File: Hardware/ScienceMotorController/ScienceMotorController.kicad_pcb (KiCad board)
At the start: 2 copper layers, 125.7 x 166.4 mm, 148 parts, among them U1 VNH5019A_E, U10 PMN280ENEAX, U11 PMN280ENEAX, U12 LT1910, U13 LT1910, U14 LT1910, U15 5VA OKI, U2 VNH5019A_E, U3 VNH5019A_E, U4 VNH5019A_E, U5 5V OKI, U6 TM4C129E_Launchpad, U7 3V3 OKI, U8 5VA OKI, U9 PMN280ENEAX

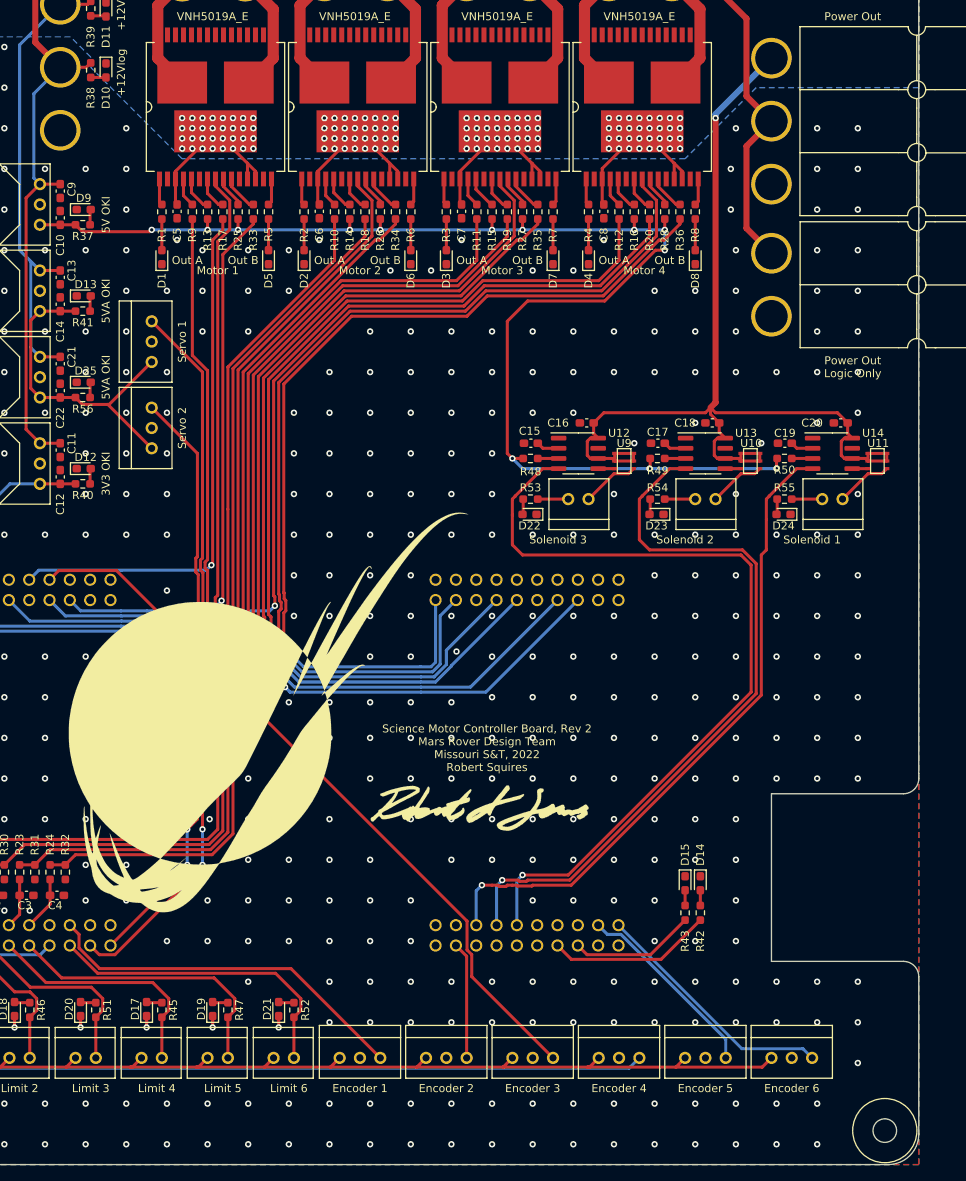
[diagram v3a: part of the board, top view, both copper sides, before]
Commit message: 9 Solenoids, Fixed PWM Overlap
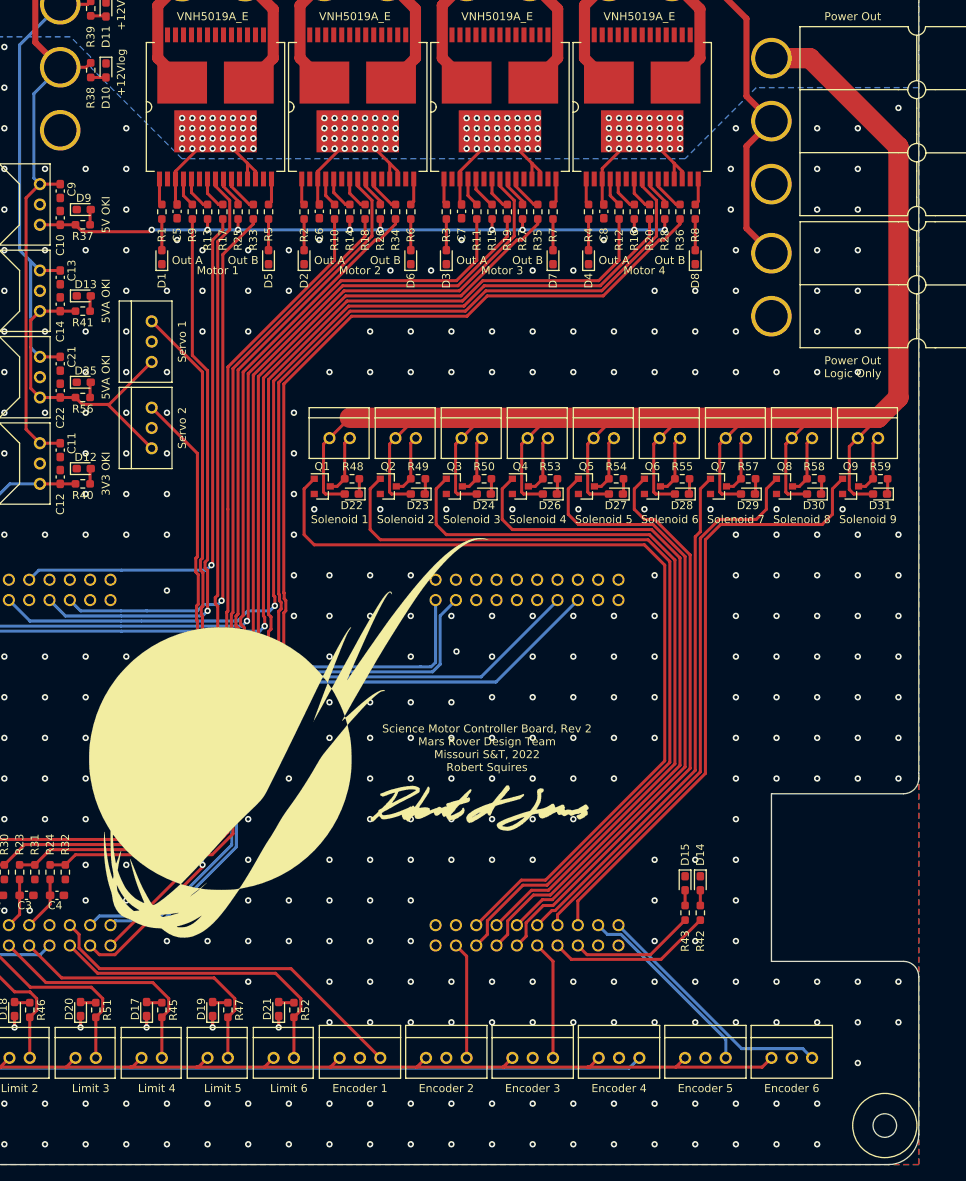
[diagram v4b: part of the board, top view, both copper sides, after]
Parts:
- removed C15, C17, C19: 0.1 uF, Capacitor_SMD:C_0603_1608Metric_Pad1.08x0.95mm_HandSolder
- removed C16, C18, C20: 10uF 50V, Capacitor_SMD:C_0603_1608Metric_Pad1.08x0.95mm_HandSolder
- removed SolValve1, SolValve2, SolValve3: Molex_SL_02, MRDT_Connectors:MOLEX_SL_02_Vertical
- removed U10, U11, U9: PMN280ENEAX, Mosfet:PMN280ENEAX
- removed U12, U13, U14: LT1910, Package_SO:SOIC-8_3.9x4.9mm_P1.27mm
- added D26: LED, LED_SMD:LED_0603_1608Metric_Pad1.05x0.95mm_HandSolder, F.Cu at (113.9, 43.2)
- added D27: LED, LED_SMD:LED_0603_1608Metric_Pad1.05x0.95mm_HandSolder, F.Cu at (122.2, 43.2)
- added D28: LED, LED_SMD:LED_0603_1608Metric_Pad1.05x0.95mm_HandSolder, F.Cu at (130.4, 43.2)
- added D29: LED, LED_SMD:LED_0603_1608Metric_Pad1.05x0.95mm_HandSolder, F.Cu at (138.7, 43.2)
- added D30: LED, LED_SMD:LED_0603_1608Metric_Pad1.05x0.95mm_HandSolder, F.Cu at (146.9, 43.2)
- added D31: LED, LED_SMD:LED_0603_1608Metric_Pad1.05x0.95mm_HandSolder, F.Cu at (155.2, 43.2)
- added Q1: BSS138, Package_TO_SOT_SMD:SOT-23, F.Cu at (85.5, 42.2)
- added Q2: BSS138, Package_TO_SOT_SMD:SOT-23, F.Cu at (93.7, 42.2)
- added Q3: BSS138, Package_TO_SOT_SMD:SOT-23, F.Cu at (102.0, 42.2)
- added Q4: BSS138, Package_TO_SOT_SMD:SOT-23, F.Cu at (110.2, 42.2)
- added Q5: BSS138, Package_TO_SOT_SMD:SOT-23, F.Cu at (118.5, 42.2)
- added Q6: BSS138, Package_TO_SOT_SMD:SOT-23, F.Cu at (126.7, 42.2)
- added Q7: BSS138, Package_TO_SOT_SMD:SOT-23, F.Cu at (135.0, 42.2)
- added Q8: BSS138, Package_TO_SOT_SMD:SOT-23, F.Cu at (143.2, 42.2)
- added Q9: BSS138, Package_TO_SOT_SMD:SOT-23, F.Cu at (151.5, 42.2)
- added R57: 1k, Resistor_SMD:R_0603_1608Metric_Pad0.98x0.95mm_HandSolder, F.Cu at (138.7, 41.3)
- added R58: 1k, Resistor_SMD:R_0603_1608Metric_Pad0.98x0.95mm_HandSolder, F.Cu at (147.0, 41.3)
- added R59: 1k, Resistor_SMD:R_0603_1608Metric_Pad0.98x0.95mm_HandSolder, F.Cu at (155.2, 41.3)
- added SolVal1: Molex_SL_02, MRDT_Connectors:MOLEX_SL_02_Vertical, F.Cu at (86.4, 36.2)
- added SolVal2: Molex_SL_02, MRDT_Connectors:MOLEX_SL_02_Vertical, F.Cu at (94.6, 36.2)
- added SolVal3: Molex_SL_02, MRDT_Connectors:MOLEX_SL_02_Vertical, F.Cu at (102.9, 36.2)
- added SolVal4: Molex_SL_02, MRDT_Connectors:MOLEX_SL_02_Vertical, F.Cu at (111.1, 36.2)
- added SolVal5: Molex_SL_02, MRDT_Connectors:MOLEX_SL_02_Vertical, F.Cu at (119.4, 36.2)
- added SolVal6: Molex_SL_02, MRDT_Connectors:MOLEX_SL_02_Vertical, F.Cu at (127.6, 36.2)
- added SolVal7: Molex_SL_02, MRDT_Connectors:MOLEX_SL_02_Vertical, F.Cu at (135.9, 36.2)
- added SolVal8: Molex_SL_02, MRDT_Connectors:MOLEX_SL_02_Vertical, F.Cu at (144.1, 36.2)
- added SolVal9: Molex_SL_02, MRDT_Connectors:MOLEX_SL_02_Vertical, F.Cu at (152.4, 36.2)
- R1, R2, R3, R4, R5, R6, R7, R8: value 1.5k -> 1k
- R48, R49, R50: value 5.1k -> 1k
- R53, R54, R55: value 130 -> 1k
- moved R50 37.6 mm to (105.7, 41.3)
- moved D24 37.6 mm to (105.7, 43.2)
- moved R49 30.0 mm to (97.4, 41.3)
- moved D23 30.0 mm to (97.4, 43.2)
- moved R48 22.4 mm to (89.2, 41.3)
- moved D22 22.4 mm to (89.1, 43.2)
- moved R55 13.0 mm to (130.5, 41.3), turned to 180 degrees
- moved R54 5.75 mm to (122.2, 41.3), turned to 180 degrees
- moved G*** 4.07 mm to (81.3, 73.7)
- moved R53 3.54 mm to (113.9, 41.3), turned to 180 degrees
- moved REF** 0.64 mm to (151.8, 118.1)
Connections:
- D22 pad 1: GND -> Net-(D22-Pad1)
- D22 pad 2: Net-(D22-Pad2) -> +12VA
- D23 pad 1: GND -> Net-(D23-Pad1)
- D23 pad 2: Net-(D23-Pad2) -> +12VA
- D24 pad 1: GND -> Net-(D24-Pad1)
- D24 pad 2: Net-(D24-Pad2) -> +12VA
- R48 pad 1: Net-(R48-Pad1) -> Net-(D22-Pad1)
- R48 pad 2: +5V -> Net-(Q1-Pad3)
- R49 pad 1: Net-(R49-Pad1) -> Net-(D23-Pad1)
- R49 pad 2: +5V -> Net-(Q2-Pad3)
- R50 pad 1: Net-(R50-Pad1) -> Net-(D24-Pad1)
- R50 pad 2: +5V -> Net-(Q3-Pad3)
- R53 pad 1: Net-(D22-Pad2) -> Net-(D26-Pad1)
- R54 pad 1: Net-(D23-Pad2) -> Net-(D27-Pad1)
- R55 pad 1: Net-(D24-Pad2) -> Net-(D28-Pad1)
- U6 pad PB5: Solenoid_Valve_2 -> Solenoid_Valve_3
- U6 pad PD0: Encoder_PWM_3 -> Net-(U6-PadPD0)
- U6 pad PD4: Net-(U6-PadPD4) -> Solenoid_Valve_6
- U6 pad PD5: Net-(U6-PadPD5) -> Encoder_PWM_3
- U6 pad PK0: Solenoid_Valve_3 -> Solenoid_Valve_5
- U6 pad PK1: Net-(U6-PadPK1) -> Solenoid_Valve_7
- U6 pad PK2: Net-(U6-PadPK2) -> Solenoid_Valve_8
- U6 pad PK3: Net-(U6-PadPK3) -> Solenoid_Valve_9
- U6 pad PM0: PWM_3 -> Net-(U6-PadPM0)
- U6 pad PM1: PWM_2 -> Net-(U6-PadPM1)
- U6 pad PM4: Net-(U6-PadPM4) -> PWM_2
- U6 pad PM5: Net-(U6-PadPM5) -> PWM_3
- U6 pad PP0: Net-(U6-PadPP0) -> Solenoid_Valve_2
- U6 pad PP1: Net-(U6-PadPP1) -> Solenoid_Valve_4
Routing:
- net +12VA: track 272.9 -> 384.2 mm, vias 129 -> 128
- net Solenoid_Valve_4: track 0.00 -> 89.0 mm
- net +5V: track 170.2 -> 89.4 mm, vias 13 -> 9
- net Encoder_PWM_3: track 92.4 -> 14.9 mm, vias 2 -> 0
- net Solenoid_Valve_5: track 0.00 -> 77.3 mm
- net Solenoid_Valve_9: track 0.00 -> 76.9 mm
- net Solenoid_Valve_6: track 0.00 -> 72.2 mm
- net Solenoid_Valve_8: track 0.00 -> 69.9 mm
- net Solenoid_Valve_7: track 0.00 -> 65.0 mm
- net Solenoid_Valve_1: track 82.4 -> 110.7 mm, vias 1 -> 0
- net Solenoid_Valve_2: track 92.0 -> 105.8 mm, vias 1 -> 0
- net Solenoid_Valve_3: track 104.6 -> 94.1 mm, vias 1 -> 0
- net PWM_3: track 112.4 -> 120.7 mm
- net Net-(Q2-Pad3): track 0.00 -> 7.55 mm
- net Net-(Q1-Pad3): track 0.00 -> 7.55 mm
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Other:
- board text added: "Solenoid 4"
- board text added: "Solenoid 5"
- board text added: "Solenoid 6"
- board text added: "Solenoid 7"
- board text added: "Solenoid 8"
- board text added: "Solenoid 9"

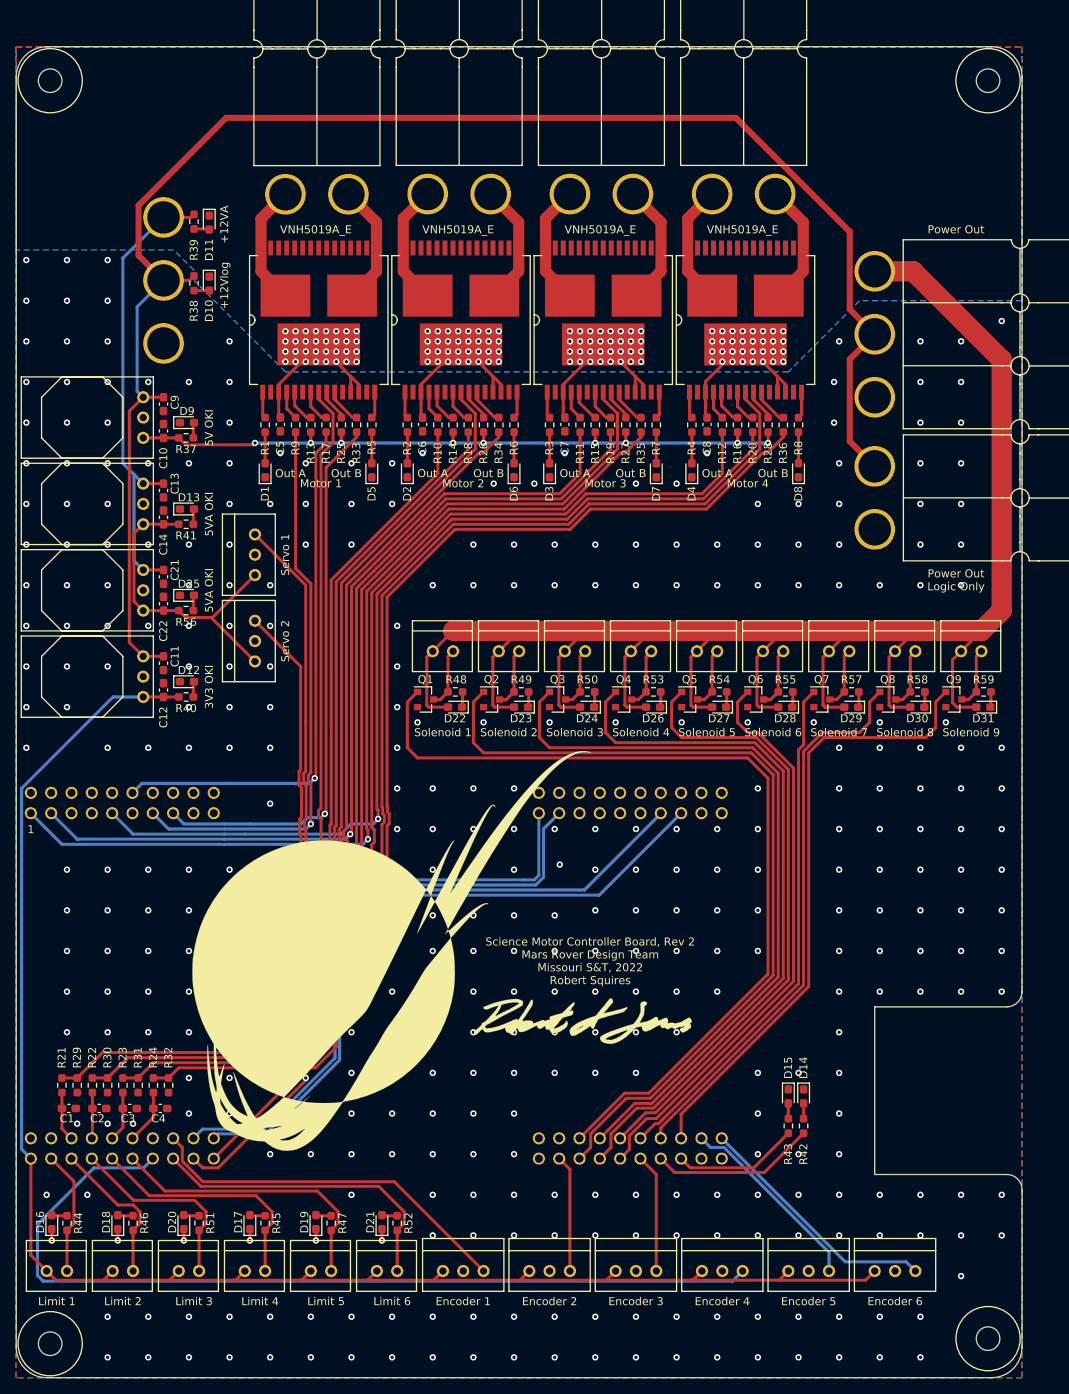
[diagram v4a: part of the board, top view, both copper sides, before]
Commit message: Removed 5V Oki, Moved +12V Passthrough Trace, Added Zener Diodes for Current Sense
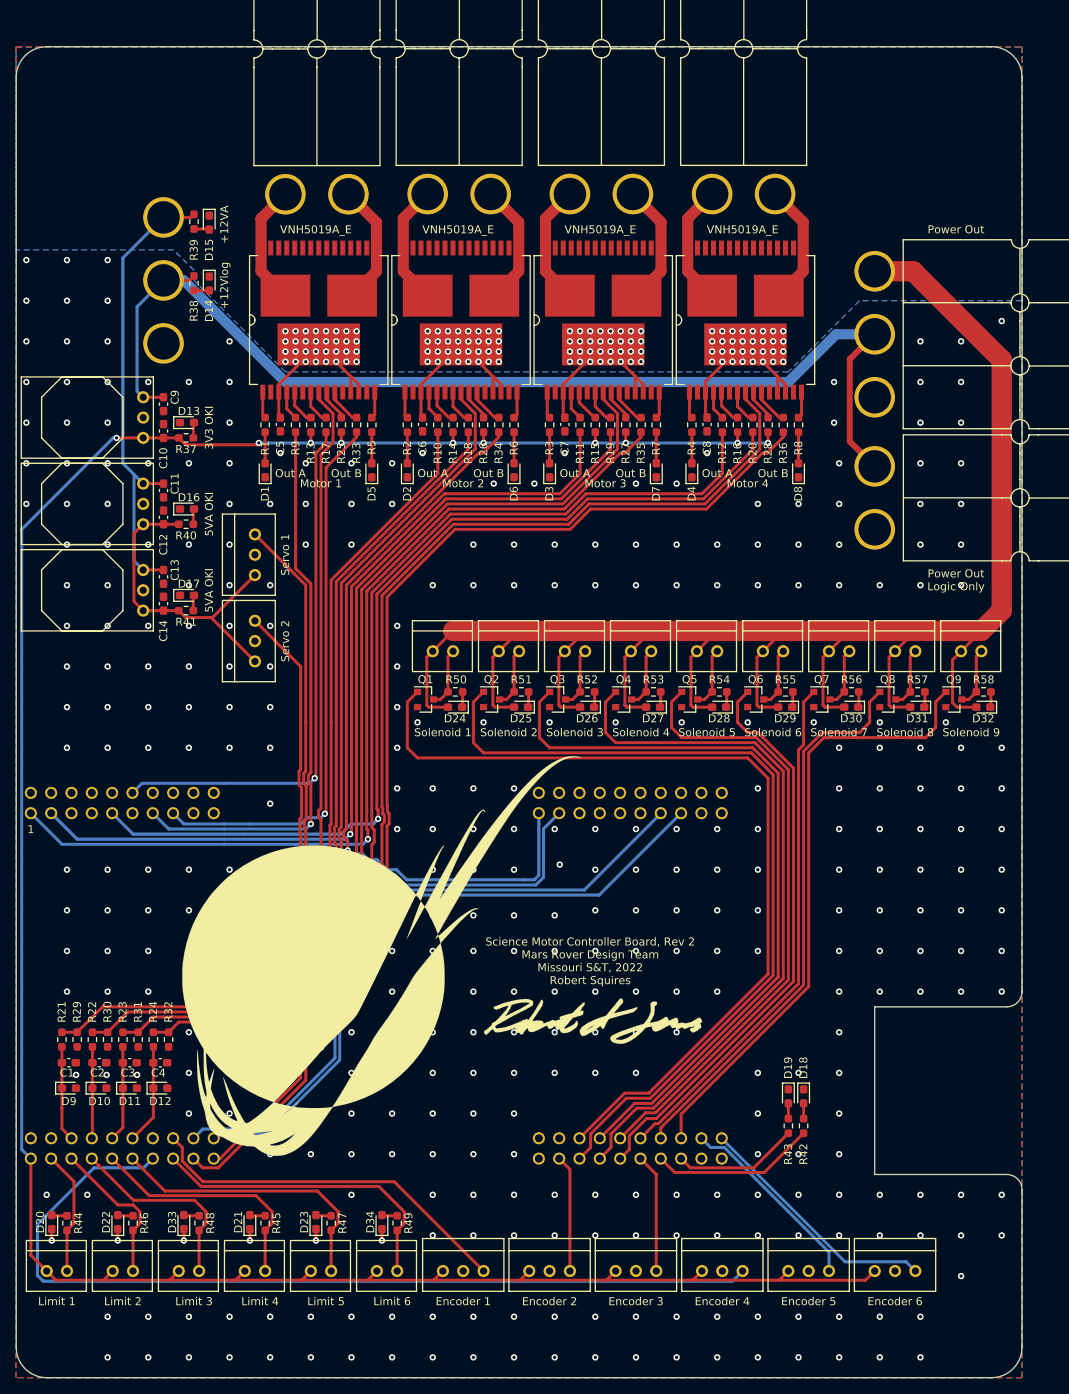
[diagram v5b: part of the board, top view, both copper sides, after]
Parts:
- removed the C11 at (52.7, 37.7)
- removed the C12 at (52.7, 41.0)
- removed the R40 at (55.5, 41.9)
- removed REF** (x4): 4_40_Hole, MRDT_Drill_Holes:4_40_Hole_Corner
- removed the U7 at (50.2, 36.8)
- added D10: 3.3V, Diode_SMD:D_0603_1608Metric_Pad1.05x0.95mm_HandSolder, F.Cu at (44.7, 90.8)
- added D11: 3.3V, Diode_SMD:D_0603_1608Metric_Pad1.05x0.95mm_HandSolder, F.Cu at (48.5, 90.8)
- added D13: LED, LED_SMD:LED_0603_1608Metric_Pad1.05x0.95mm_HandSolder, F.Cu at (55.6, 7.62)
- D12, D9: value LED -> 3.3V; footprint LED_SMD:LED_0603_1608Metric_Pad1.05x0.95mm_HandSolder -> Diode_SMD:D_0603_1608Metric_Pad1.05x0.95mm_HandSolder
- R37: value 300 -> 130
- U5: value 5V OKI -> 3V3 OKI
- moved D9 84.5 mm to (40.9, 90.8)
- moved D12 50.9 mm to (52.3, 90.8)
- moved C1 5.72 mm to (40.9, 87.6)
- moved C2 5.72 mm to (44.7, 87.6)
- moved C3 5.72 mm to (48.5, 87.6)
- moved C4 5.72 mm to (52.3, 87.6)
- moved R21 5.72 mm to (40.0, 84.7)
- moved R22 5.72 mm to (43.8, 84.7)
- moved R23 5.72 mm to (47.6, 84.7)
- moved R24 5.72 mm to (51.4, 84.7)
- moved R29 5.72 mm to (41.9, 84.7)
- moved R30 5.72 mm to (45.7, 84.7)
- moved R31 5.72 mm to (49.5, 84.7)
- moved R32 5.72 mm to (53.3, 84.7)
- moved G*** 1.42 mm to (80.0, 74.3)
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- renumbered AbsEncode4 to AbsEncode2, AbsEncode2 to AbsEncode3, AbsEncode5 to AbsEncode4, AbsEncode3 to AbsEncode5, C13 to C11, C14 to C12, C21 to C13, C22 to C14, D10 to D14, D11 to D15, D13 to D16, D25 to D17, D14 to D18, D15 to D19, D16 to D20, D17 to D21, D18 to D22, D19 to D23, D22 to D24, D23 to D25, D24 to D26, D26 to D27, D27 to D28, D28 to D29, D29 to D30, D30 to D31, D31 to D32, D20 to D33, D21 to D34, LimSwitch4 to LimSwitch2, LimSwitch2 to LimSwitch3, LimSwitch5 to LimSwitch4, LimSwitch3 to LimSwitch5, R41 to R40, R56 to R41, R51 to R48, R52 to R49, R48 to R50, R49 to R51, R50 to R52, R57 to R56, R58 to R57, R59 to R58, U8 to U7, U15 to U8
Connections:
- C10 pad 1: +5V -> +3V3
- D12 pad 1: GND -> Current_Sense_4
- D12 pad 2: Net-(D12-Pad2) -> GND
- D9 pad 1: GND -> Current_Sense_1
- D9 pad 2: Net-(D9-Pad2) -> GND
- R13 pad 2: +5V -> +3V3
- R14 pad 2: +5V -> +3V3
- R15 pad 2: +5V -> +3V3
- R16 pad 2: +5V -> +3V3
- R25 pad 2: +5V -> +3V3
- R26 pad 2: +5V -> +3V3
- R27 pad 2: +5V -> +3V3
- R28 pad 2: +5V -> +3V3
- R37 pad 1: Net-(D9-Pad2) -> Net-(D13-Pad2)
- R37 pad 2: +5V -> +3V3
- U5 pad 3: +5V -> +3V3
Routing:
- net +3V3: track 207.5 -> 324.8 mm, vias 0 -> 10
- net +5V: track 89.4 -> 0.00 mm, vias 9 -> 0
- net +12V: track 202.4 -> 138.6 mm
- net Net-(R24-Pad1): track 146.2 -> 140.5 mm
- net Net-(R23-Pad1): track 133.6 -> 127.9 mm
- net Net-(R22-Pad1): track 121.1 -> 115.4 mm
- net Net-(R21-Pad1): track 117.1 -> 111.4 mm
- net Current_Sense_4: track 6.80 -> 12.5 mm
- net Current_Sense_3: track 6.27 -> 12.0 mm
- net Current_Sense_1: track 6.21 -> 11.9 mm
- net Current_Sense_2: track 5.75 -> 11.5 mm
- net Net-(D9-Pad2): track 1.94 -> 0.00 mm
- net Net-(D13-Pad2): track 0.00 -> 1.94 mm
- net Net-(D12-Pad2): track 1.94 -> 0.00 mm
- net Servo_2: track 74.4 -> 75.4 mm
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
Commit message: ok but actually this time
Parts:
- Conn1, Conn2, Conn3, Conn4, Conn7: footprint MRDT_Connectors:Anderson_2_Horizontal_Side_by_Side -> MRDT_Connectors:Square_Anderson_2_H_Side_By_Side
- Conn5, Conn6: footprint MRDT_Connectors:Anderson_3_Horizontal_Side_by_Side -> MRDT_Connectors:Square_Anderson_3_H_Side_By_Side
- moved Conn6 7.65 mm to (142.2, -3.17)
- moved Conn5 7.10 mm to (52.6, -9.39)
